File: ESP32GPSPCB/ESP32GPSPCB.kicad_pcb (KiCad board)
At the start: 4 copper layers, 75 x 130 mm, 67 parts, among them J1 Conn_01x04_Socket, J2 USB_C_Receptacle_USB2.0_14P, J3 Conn_01x14_Socket, J4 Conn_01x04_Socket, J5 Boot Option, J6 Conn_01x04_Socket, J7 Conn_01x05_Socket, J8 Logic extra channel, J9 Battery Input, SW1 SW_Push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

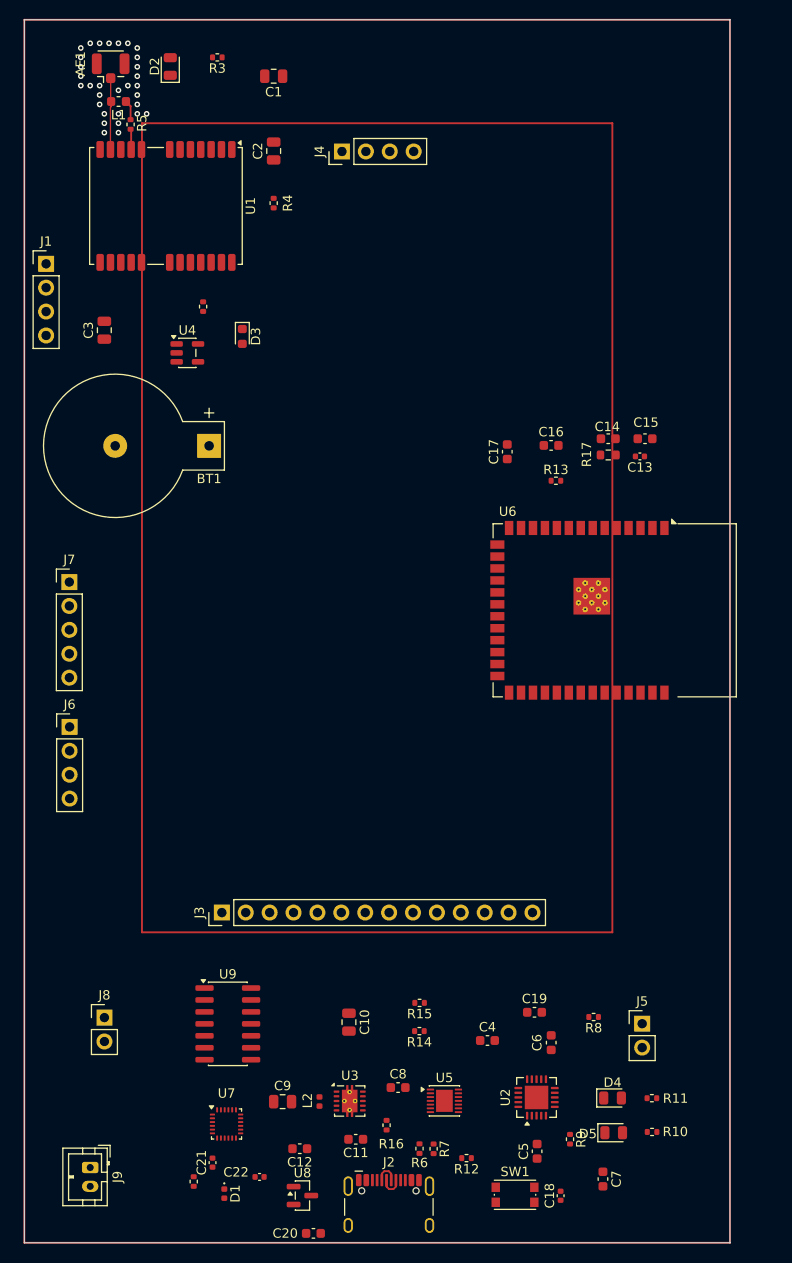
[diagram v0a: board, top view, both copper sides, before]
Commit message: routed some of the parts
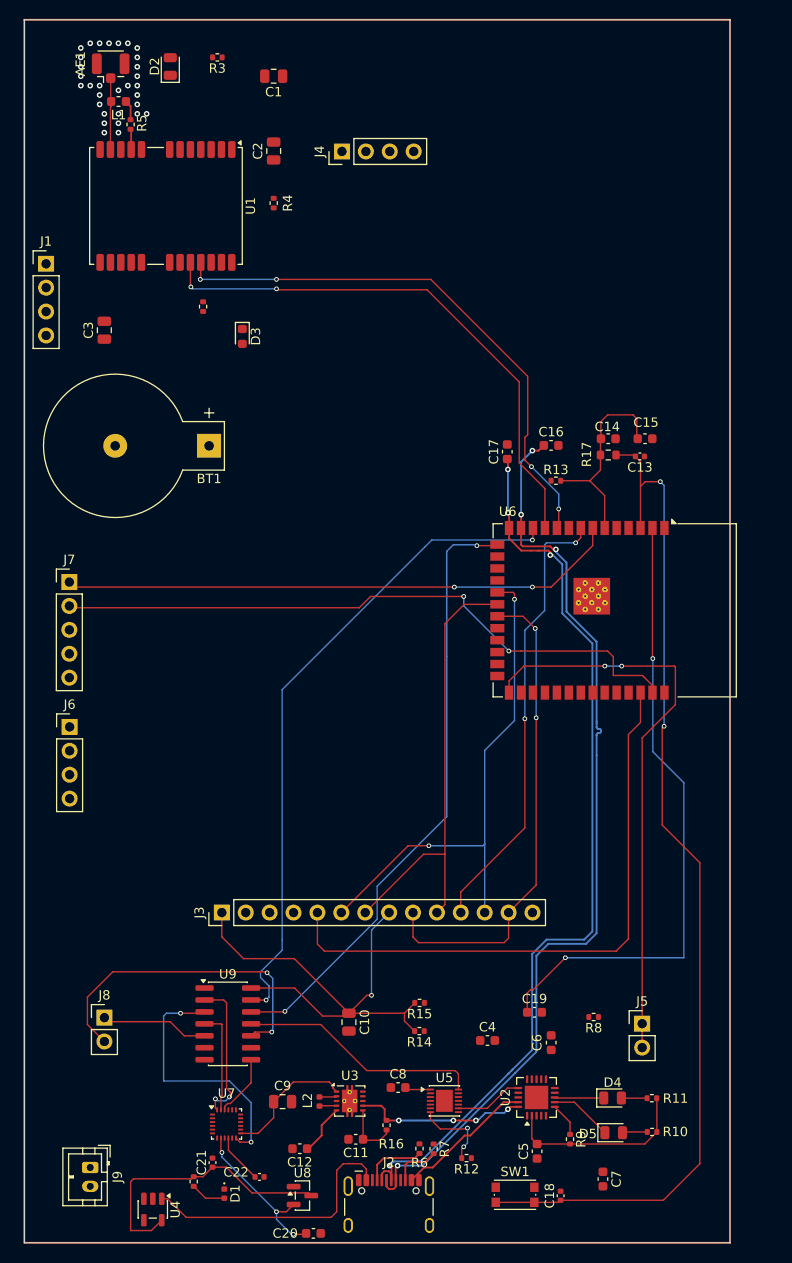
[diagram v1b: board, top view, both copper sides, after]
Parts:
- moved U4 91.1 mm to (85.7, 163.5), turned to -90 degrees
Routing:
- net +3V3: track 0.00 -> 187.2 mm, vias 0 -> 3
- net /ESP32_EN: track 0.00 -> 110.1 mm, vias 0 -> 2
- net /D-: track 2.59 -> 100.6 mm, vias 0 -> 4
- net /D+: track 2.59 -> 97.9 mm, vias 0 -> 4
- net /I2C_SDA: track 0.00 -> 70.5 mm, vias 0 -> 2
- net /GPIO1: track 0.00 -> 69.0 mm, vias 0 -> 2
- net /GPIO3: track 0.00 -> 65.4 mm, vias 0 -> 2
- net /TFT_DC: track 0.00 -> 64.0 mm
- net +5V: track 0.00 -> 63.8 mm
- net Net-(J5-Pin_2): track 0.00 -> 61.6 mm, vias 0 -> 2
- net /GPIO7: track 0.00 -> 59.5 mm, vias 0 -> 2
- net /GPS_RX: track 0.00 -> 58.7 mm, vias 0 -> 4
- net /GPS_TX: track 0.00 -> 58.4 mm, vias 0 -> 2
- net /SPI_MOSI: track 0.00 -> 55.4 mm, vias 0 -> 2
- net /SPI_MISO: track 0.00 -> 52.0 mm, vias 0 -> 2
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
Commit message: Routed all traces and poured copper planes, GND, +1V8, VSYS, +3V3
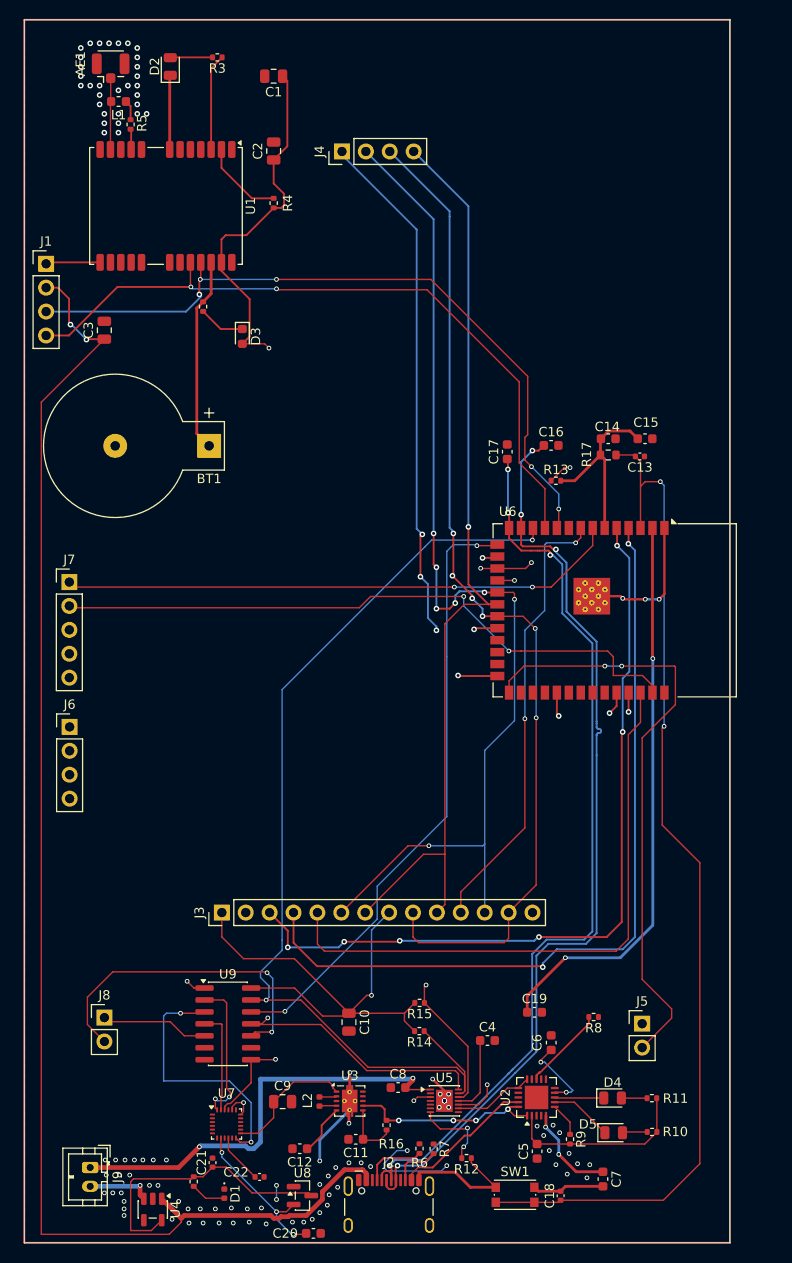
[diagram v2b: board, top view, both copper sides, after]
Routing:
- net +5V: track 63.8 -> 193.8 mm, vias 0 -> 4
- net /I2C_SCL: track 25.9 -> 130.0 mm, vias 0 -> 4
- net GND: track 0.00 -> 97.2 mm, vias 0 -> 25
- net /TFT_RST: track 0.00 -> 85.9 mm, vias 0 -> 2
- net /TFT_CS: track 0.00 -> 83.9 mm, vias 0 -> 6
- net /BAT_ALRT: track 0.00 -> 74.9 mm, vias 0 -> 2
- net Net-(J6-Pin_3): track 0.00 -> 66.0 mm, vias 0 -> 1
- net Net-(J6-Pin_2): track 0.00 -> 63.2 mm, vias 0 -> 1
- net /SD_CS: track 0.00 -> 61.8 mm, vias 0 -> 4
- net /SPI_MOSI: track 55.4 -> 115.1 mm, vias 2 -> 7
- net /GPIO38: track 0.00 -> 57.0 mm, vias 0 -> 1
- net /VBAT: track 10.0 -> 65.3 mm, vias 0 -> 4
- net /SPI_MISO: track 52.0 -> 107.1 mm, vias 2 -> 6
- net /SPI_CLK: track 48.5 -> 100.9 mm, vias 0 -> 1
- net /GPIO46: track 0.00 -> 48.7 mm, vias 0 -> 1
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- added copper zone on In2.Cu, net +3V3
- added copper zone on In2.Cu, net /+1V8
- added copper zone on In2.Cu, net /VSYS
- added copper zone on B.Cu, net GND
- added copper zone on F.Cu, net GND
- added copper zone on In1.Cu, net GND

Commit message: added designs and silkscreens
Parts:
- SW1: value SW_Push -> RST
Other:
- board text added: "+5V"
- board text added: "--------TOUCH--------"
- board text added: "3V3"
- board text added: "A4"
- board text added: "B4"
- board text added: "Designer: Muhammad Uzzam butt ©️ 2026"
- board text added: "ESP32 GPS MAPS"
- board text added: "GND"
- board text added: "GPIO0"
- board text added: "GPIO1"
- board text added: "GPIO38"
- board text added: "GPIO45"
- board text added: "GPIO46"
- board text added: "GPIO7"
- board text added: "GPS_RX"
- board text added: "GPS_TX"
- board text added: "LED"
- board text added: "NORTHERNSTUDIOS.CC"
- board text added: "RXDO"
- board text added: "SD_CS"
- board text added: "SPI_CLK"
- board text added: "SPI_MISO"
- board text added: "SPI_MOSI"
- board text added: "TFT_CS"
- board text added: "TFT_DC"
- board text added: "TFT_RST"
- board text added: "TXDO"
- board text added: "T_CS"
- board text added: "T_IRQ"
- board text added: "T_SPI_MISO"
- board text added: "T_SPI_MOSI"

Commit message: fix
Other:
- board text added: "Designer: Muhammad Uzzam Butt ©️ 2026"
- board text removed: "Designer: Muhammad Uzzam butt ©️ 2026"
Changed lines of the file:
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@@
 		)
 	)
-	(gr_text "Designer: Muhammad Uzzam butt ©️ 2026"
+	(gr_text "Designer: Muhammad Uzzam Butt ©️ 2026"
 		(at 111.9 45.2 0)
 		(layer "F.SilkS")

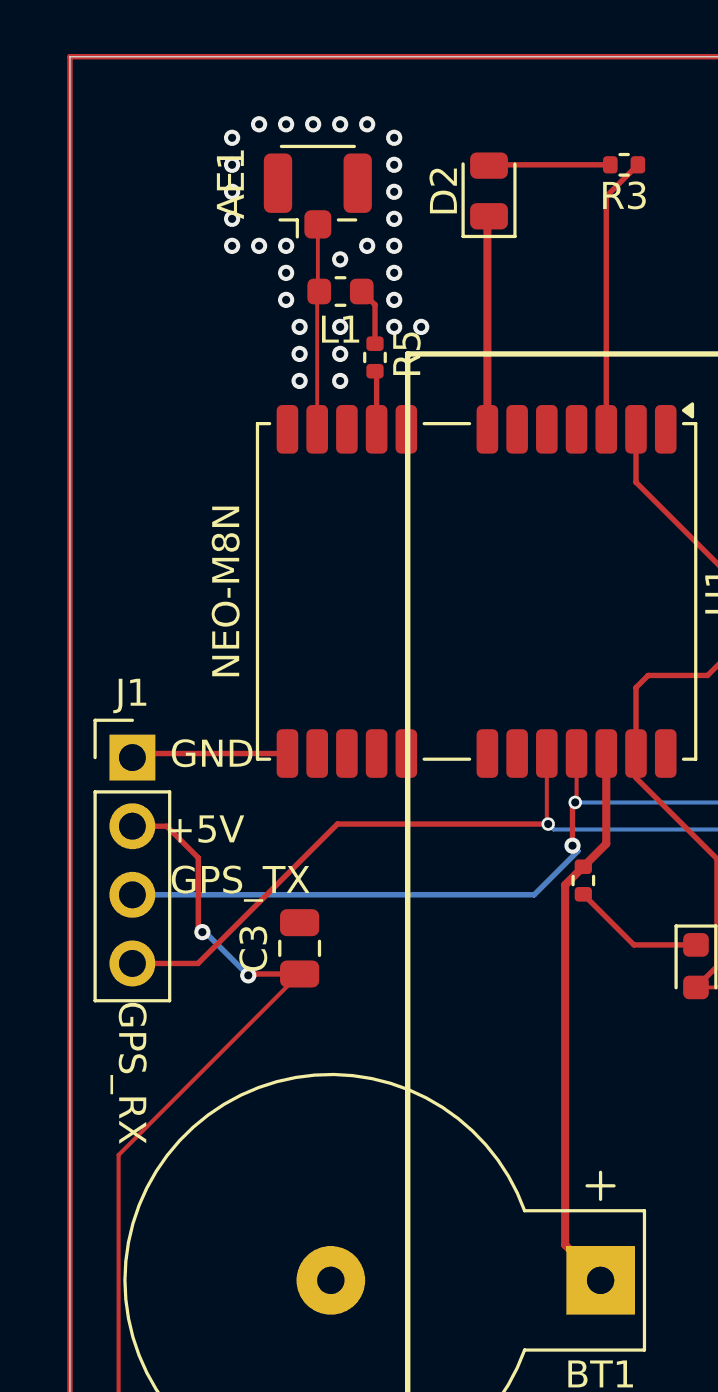
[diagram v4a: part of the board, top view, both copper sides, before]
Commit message: power plane fixes
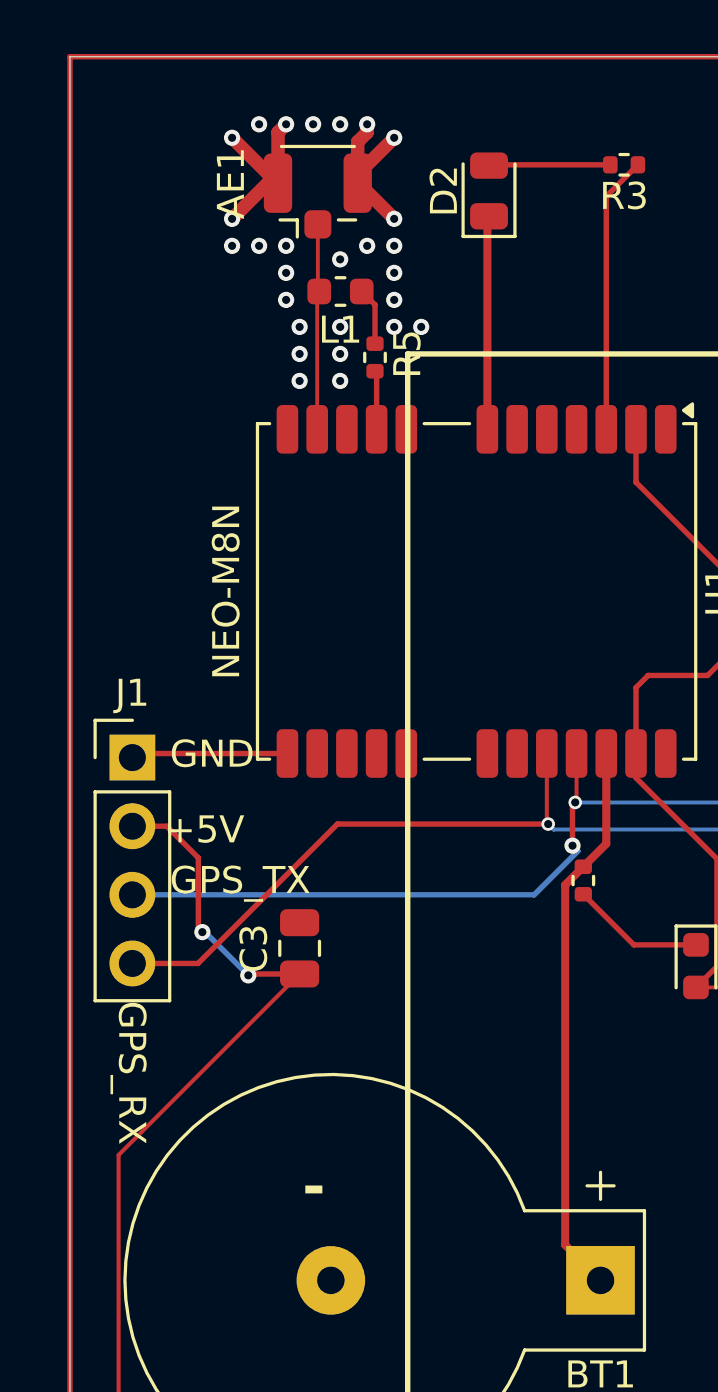
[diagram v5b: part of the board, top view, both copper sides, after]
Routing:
- net GND: track 97.2 -> 110.6 mm, vias 25 -> 31
- net (no net): vias 87 -> 77
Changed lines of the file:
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@@
+		)
+	)
+	(gr_text "-"
+		(at 80.6 79.7 0)
+		(layer "F.SilkS")
+		(effects
+			(font
+				(size 1.5 1.5)
+				(thickness 0.3)
+				(bold yes)
+			)
+			(justify left bottom)
 		)
 	)
@@
 	)
 	(via
-		(at 84 41)
-		(size 0.6)
-		(drill 0.3)
-		(layers "F.Cu" "B.Cu")
-		(net 0)
-	)
-	(via
 		(at 82 44.5)
 		(size 0.6)
@@
 	)
 	(via
-		(at 78 42)
-		(size 0.6)
-		(drill 0.3)
-		(layers "F.Cu" "B.Cu")
-		(net 0)
-	)
-	(via
 		(at 80.6 158.2)
 		(size 0.5)
@@
 	)
 	(via
-		(at 84 43)
-		(size 0.6)
-		(drill 0.3)
-		(layers "F.Cu" "B.Cu")
-		(net 0)
-	)
-	(via
 		(at 128.9 155.3)
 		(size 0.5)
@@
 	)
 	(via
-		(at 78 43)
-		(size 0.6)
-		(drill 0.3)
-		(layers "F.Cu" "B.Cu")
-		(net 0)
-	)
-	(via
 		(at 81.4 161.7)
 		(size 0.5)
@@
 	)
 	(via
-		(at 84 40)
-		(size 0.6)
-		(drill 0.3)
-		(layers "F.Cu" "B.Cu")
-		(net 0)
-	)
-	(via
 		(at 82.1 159.8)
 		(size 0.5)
@@
 	)
 	(via
-		(at 83 39.5)
-		(size 0.6)
-		(drill 0.3)
-		(layers "F.Cu" "B.Cu")
-		(net 0)
-	)
-	(via
-		(at 84 42)
-		(size 0.6)
-		(drill 0.3)
-		(layers "F.Cu" "B.Cu")
-		(net 0)
-	)
-	(via
 		(at 101.7 164.8)
 		(size 0.5)
@@
 	)
 	(via
-		(at 78 41)
-		(size 0.6)
-		(drill 0.3)
-		(layers "F.Cu" "B.Cu")
-		(net 0)
-	)
-	(via
 		(at 82 39.5)
 		(size 0.6)
@@
 	)
 	(via
-		(at 80 39.5)
-		(size 0.6)
-		(drill 0.3)
-		(layers "F.Cu" "B.Cu")
-		(net 0)
-	)
-	(via
 		(at 100.5 164.8)
 		(size 0.5)
@@
 		(at 92.3 163.4)
 		(size 0.5)
-		(drill 0.3)
-		(layers "F.Cu" "B.Cu")
-		(net 0)
-	)
-	(via
-		(at 78 40)
-		(size 0.6)
 		(drill 0.3)
 		(layers "F.Cu" "B.Cu")
@@
 	)
 	(segment
+		(start 79.7 41.68)
+		(end 79.68 41.68)
+		(width 0.5)
+		(layer "F.Cu")
+		(net 2)
+	)
+	(segment
+		(start 82.65 40.15)
+		(end 82.65 41.68)
+		(width 0.5)
+		(layer "F.Cu")
+		(net 2)
+	)
+	(segment
 		(start 135.6 98.5)
 		(end 135.3712 98.2712)
@@
 	)
 	(segment
+		(start 79.7 41.68)
+		(end 79.32 41.68)
+		(width 0.5)
+		(layer "F.Cu")
+		(net 2)
+	)
+	(segment
+		(start 83 39.8)
+		(end 82.65 40.15)
+		(width 0.5)
+		(layer "F.Cu")
+		(net 2)
+	)
+	(segment
+		(start 82.65 41.35)
+		(end 84 40)
+		(width 0.5)
+		(layer "F.Cu")
+		(net 2)
+	)
+	(segment
 		(start 113.7884 151.5116)
 		(end 115.1615 151.5116)
@@
 	)
 	(segment
+		(start 79.7 39.8)
+		(end 79.7 41.68)
+		(width 0.5)
+		(layer "F.Cu")
+		(net 2)
+	)
+	(segment
 		(start 115.4 149.6)
 		(end 116.649 150.849)
@@
 	)
 	(segment
+		(start 80 39.5)
+		(end 79.7 39.8)
+		(width 0.5)
+		(layer "F.Cu")
+		(net 2)
+	)
+	(segment
 		(start 84.3 160.9)
 		(end 84.3 161.925)
@@
 	)
 	(segment
+		(start 82.65 41.68)
+		(end 82.65 41.35)
+		(width 0.5)
+		(layer "F.Cu")
+		(net 2)
+	)
+	(segment
 		(start 94.09 152.538096)
 		(end 94.09 152.87)
@@
 	)
 	(segment
+		(start 83 39.5)
+		(end 83 39.8)
+		(width 0.5)
+		(layer "F.Cu")
+		(net 2)
+	)
+	(segment
+		(start 79.32 41.68)
+		(end 78 43)
+		(width 0.5)
+		(layer "F.Cu")
+		(net 2)
+	)
+	(segment
 		(start 138 98.6)
 		(end 135.7 98.6)
@@
 	)
 	(segment
+		(start 79.68 41.68)
+		(end 78 40)
+		(width 0.5)
+		(layer "F.Cu")
+		(net 2)
+	)
+	(segment
 		(start 117.8 159.5)
 		(end 119.3996 161.0996)
@@
 	)
 	(segment
+		(start 82.68 41.68)
+		(end 84 43)
+		(width 0.5)
+		(layer "F.Cu")
+		(net 2)
+	)
+	(segment
 		(start 129.52 161)
 		(end 129 161.52)
@@
 	)
 	(segment
+		(start 82.65 41.68)
+		(end 82.68 41.68)
+		(width 0.5)
+		(layer "F.Cu")
+		(net 2)
+	)
+	(segment
 		(start 126.6256 161.52)
 		(end 126.2052 161.0996)
@@
 	)
 	(via
+		(at 84 43)
+		(size 0.6)
+		(drill 0.3)
+		(layers "F.Cu" "B.Cu")
+		(net 2)
+	)
+	(via
 		(at 117.1 152.6)
 		(size 0.5)
@@
 	)
 	(via
+		(at 78 43)
+		(size 0.6)
+		(drill 0.3)
+		(layers "F.Cu" "B.Cu")
+		(net 2)
+	)
+	(via
 		(at 103.4 158.3)
 		(size 0.5)
@@
 	)
 	(via
+		(at 84 40)
+		(size 0.6)
+		(drill 0.3)
+		(layers "F.Cu" "B.Cu")
+		(free yes)
+		(net 2)
+	)
+	(via
 		(at 121.2 150.2)
 		(size 0.5)
@@
 	)
 	(via
+		(at 83 39.5)
+		(size 0.6)
+		(drill 0.3)
+		(layers "F.Cu" "B.Cu")
+		(net 2)
+	)
+	(via
 		(at 98.8 162.4)
 		(size 0.5)
@@
 	)
 	(via
+		(at 80 39.5)
+		(size 0.6)
+		(drill 0.3)
+		(layers "F.Cu" "B.Cu")
+		(net 2)
+	)
+	(via
 		(at 116.649 151.9116)
 		(size 0.5)
@@
 		(net 2)
 	)
+	(via
+		(at 78 40)
+		(size 0.6)
+		(drill 0.3)
+		(layers "F.Cu" "B.Cu")
+		(free yes)
+		(net 2)
+	)
